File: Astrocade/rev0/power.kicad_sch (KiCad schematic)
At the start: 10 parts, among them U5 AP63203WU

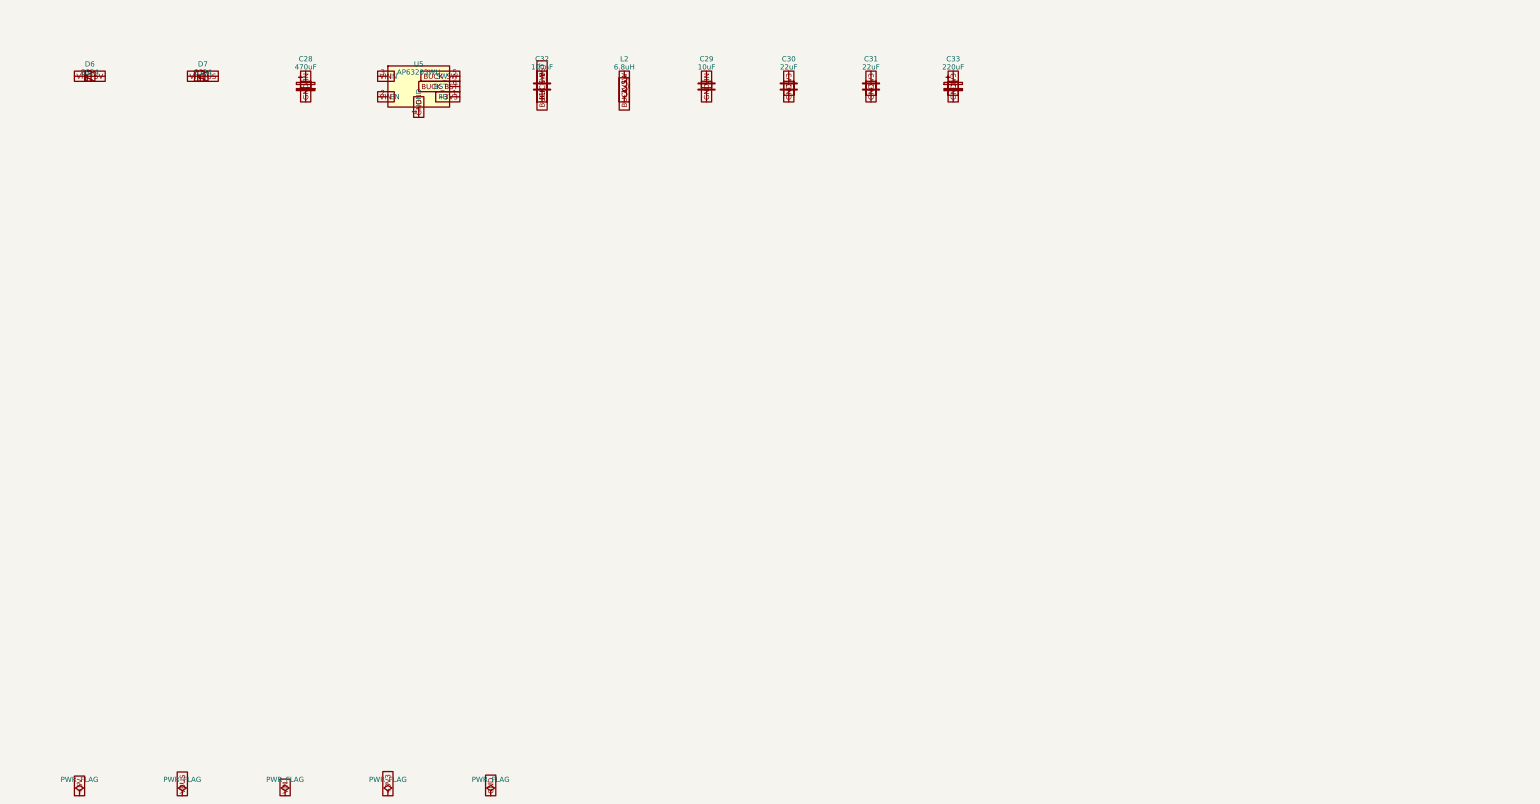
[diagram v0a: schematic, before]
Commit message: Astrocade Rev0: redo on RP2354A + ESP32-S3, 6-layer, fully autorouted
Replaces the unrouted RP2040 + 3x LVC245 draft with an INTV-style board:
RP2354A straight on the 5V bus, ESP32-S3-WROOM-1-N16R8 as its USB host
(PICOBOOT reflash), USB-C/CP2102N, push-push microSD, WS2812B-2020-V6,
RESET/BOOTSEL/EN/BOOT buttons. Same cassette outline, lands and holes.

Everything is generated by tools/ (build_all.sh): design.py -> schematic,
placement + plane fan-out, Raspberry Pi's MIT regulator-corner graft,
Freerouting + A* finisher, netlist-vs-firmware check, JLCPCB BOM/CPL/gerbers.
ERC 0, DRC 0 errors / 0 unconnected / 0 parity, check_nets 174/174.

RUN/BOOTSEL from the S3 are direct 1k links (fnPicoUpdater drives them low;
an NPN driver would invert it). Shell openings come from the placement.

Co-Authored-By: Claude Opus 5.5 (1M context) <noreply@anthropic.com>
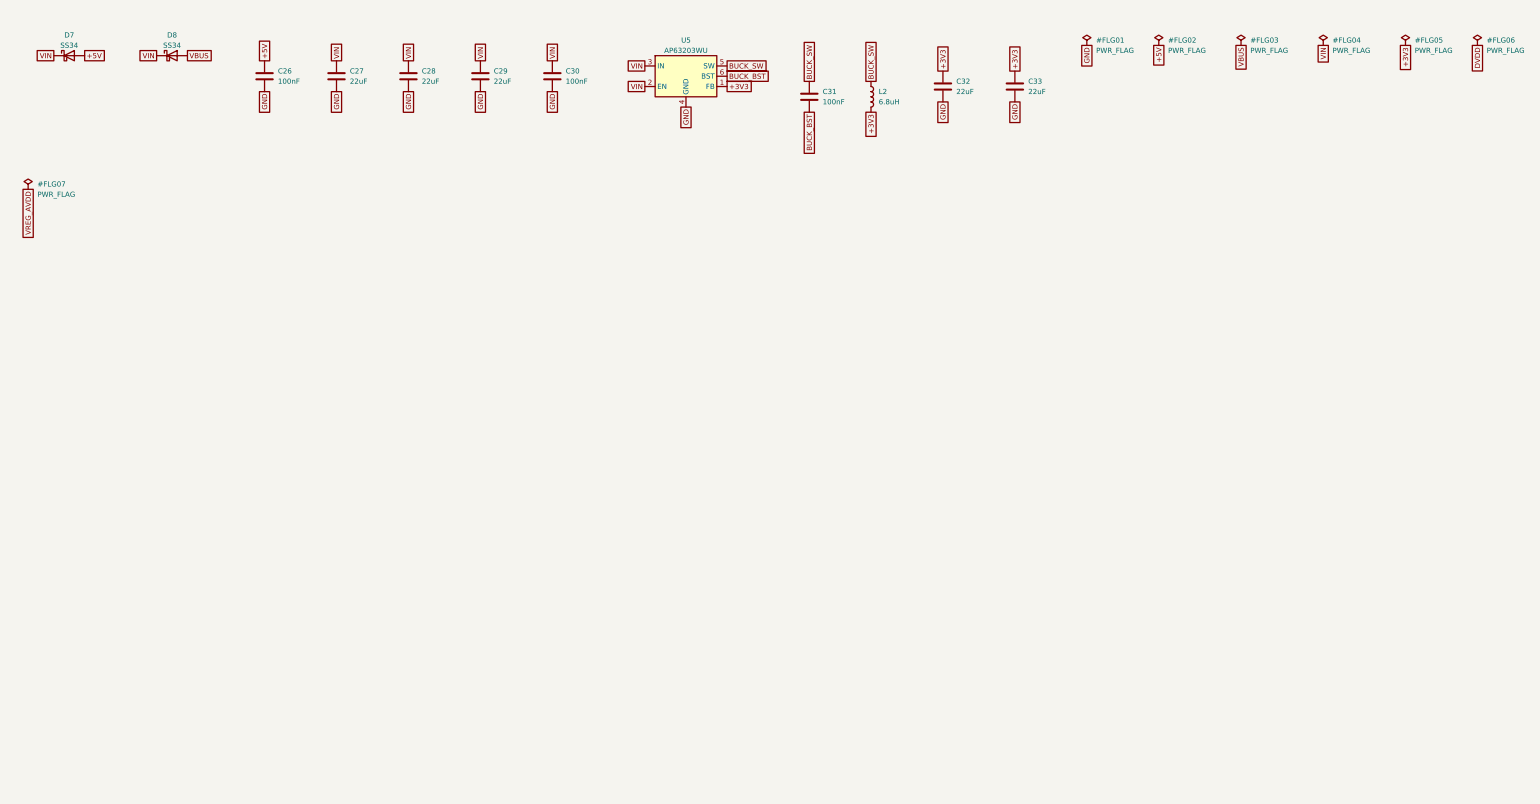
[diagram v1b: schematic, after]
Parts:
- removed C28: 470uF, FujiNet-Astrocade:CP_EIA-7343-31_Kemet-D, symbol Device:C_Polarized
- removed C33: 220uF, FujiNet-Astrocade:CP_EIA-7343-31_Kemet-D, symbol Device:C_Polarized
- removed D6: SS34, FujiNet-Astrocade:D_SMA, symbol Diode:SS34
- added C26: 100nF, FujiNet-Astrocade:C_0603_1608Metric, symbol Device:C
- added C27, C28, C33: 22uF, FujiNet-Astrocade:C_0805_2012Metric, symbol Device:C
- added D8: SS34, FujiNet-Astrocade:D_SMA, symbol Diode:SS34
- C29: value 10uF -> 22uF; LCSC (none) -> C45783; MPN (none) -> CL21A226MAQNNNE
- C30, C31: value 22uF -> 100nF; footprint FujiNet-Astrocade:C_0805_2012Metric -> FujiNet-Astrocade:C_0603_1608Metric; LCSC C45783 -> C14663; MPN (none) -> CC0603KRX7R9BB104
- C32: value 100nF -> 22uF; footprint FujiNet-Astrocade:C_0603_1608Metric -> FujiNet-Astrocade:C_0805_2012Metric; LCSC (none) -> C45783; MPN (none) -> CL21A226MAQNNNE
- D7: MPN (none) -> SS34
- L2: LCSC (none) -> C62684; MPN 6.8uH >=2.5A shielded 4030 -> SWPA4030S6R8MT
- U5: LCSC C965680 -> C780769
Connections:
- net +3V3: now also C32.1, C33.1; no longer C30.1, C31.1
- net +5V: now also D7.2 (A), C26.1
- net BUCK_BST: now also C31.2; no longer C32.2
- net BUCK_SW: now also C31.1; no longer C32.1
- net GND: now also C32.2, C26.2, C27.2, C28.2, C33.2; no longer C31.2
- net VBUS: now also D8.2 (A); no longer D7.2 (A)
- net VIN: now also C30.1, C27.1, C28.1, D8.1 (K)
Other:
- company: (none) -> FujiNet
- title: (none) -> FujiNet Astrocade Rev0 - Power: console 5V / USB VBUS OR, 3.3V buck

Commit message: Astrocade Rev0: audit with kicad-happy + datasheets and redo
Schematic, board and fab outputs regenerated from tools/ after a
datasheet-level audit (docs/design-review-rev0.md).

Design fixes:
- RP2354A on its own AP2112K rail (+3V3_RP): its FT pads take 5.5 V only
  with IOVDD powered (RP2350 DS p.1332); the buck's UVLO + 4 ms soft-start
  left them unpowered while the console drove the bus
- WS2812B-2020-V6 on +5V (datasheet VDD 3.7-5.3 V, not a 3.3 V part)
- VBUS decoupling at the USB-C, activity LED 330R, card-detect polarity
  settled (low = card present), fiducials, RUN/BOOTSEL/rail test pads

Schematic redrawn readably: root block diagram with hierarchical pins,
power symbols, wired clusters and design notes (tools/sch_layout.py);
check_sch_layout.py proves the drawn netlist equals design.py.

Board: 4 layers tried first and did not close; 6 layers, 100% routed,
DRC 0 errors / 0 unconnected / 0 parity. Locked USB-C D+/D- pad ties,
GND stitching kept out of pads, return vias at USB/crystal layer
changes, check_vias.py gate (KiCad re-nets a via inside another net's
pad, so its DRC cannot see it).

Co-Authored-By: Claude Opus 5.5 <noreply@anthropic.com>
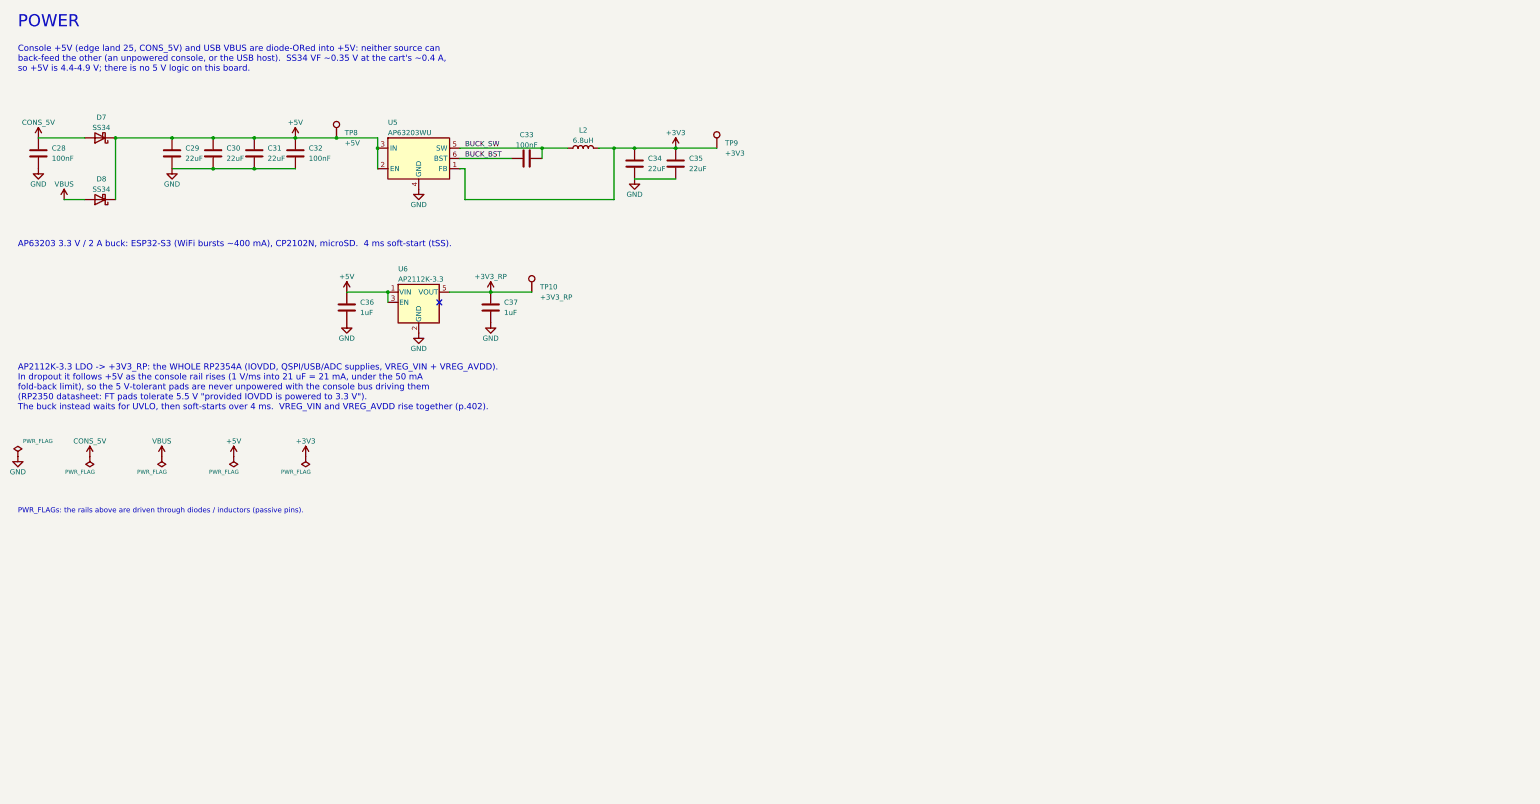
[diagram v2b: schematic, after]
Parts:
- removed C26: 100nF, FujiNet-Astrocade:C_0603_1608Metric, symbol Device:C
- removed C27: 22uF, FujiNet-Astrocade:C_0805_2012Metric, symbol Device:C
- added C34, C35: 22uF, FujiNet-Astrocade:C_0805_2012Metric, symbol Device:C
- added C36, C37: 1uF, FujiNet-Astrocade:C_0603_1608Metric, symbol Device:C
- added TP10: +3V3_RP, FujiNet-Astrocade:TestPoint_Pad_D1.5mm, symbol Connector:TestPoint
- added TP8: +5V, FujiNet-Astrocade:TestPoint_Pad_D1.5mm, symbol Connector:TestPoint
- added TP9: +3V3, FujiNet-Astrocade:TestPoint_Pad_D1.5mm, symbol Connector:TestPoint
- added U6: AP2112K-3.3, FujiNet-Astrocade:SOT-23-5, symbol Regulator_Linear:AP2112K-3.3
- C28, C32, C33: value 22uF -> 100nF; footprint FujiNet-Astrocade:C_0805_2012Metric -> FujiNet-Astrocade:C_0603_1608Metric; LCSC C45783 -> C14663; MPN CL21A226MAQNNNE -> CC0603KRX7R9BB104
- C30, C31: value 100nF -> 22uF; footprint FujiNet-Astrocade:C_0603_1608Metric -> FujiNet-Astrocade:C_0805_2012Metric; LCSC C14663 -> C45783; MPN CC0603KRX7R9BB104 -> CL21A226MAQNNNE
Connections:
- net +3V3: now also C34.1, C35.1, TP9.1; no longer C32.1, C33.1
- net +5V: now also C29.1, C30.1, C31.1, C32.1, D7.1 (K), D8.1 (K), U5.2 (EN), U5.3 (IN), C36.1, TP8.1, U6.1 (VIN), U6.3 (EN); no longer D7.2 (A)
- net BUCK_BST: now also C33.2; no longer C31.2
- net BUCK_SW: now also C33.1; no longer C31.1
- net GND: now also C31.2, C34.2, C35.2, C36.2, C37.2, U6.2 (GND); no longer C33.2
- removed net VIN: C28.1, C29.1, C30.1, D7.1 (K), D8.1 (K), U5.2 (EN), U5.3 (IN)
- new net +3V3_RP: C37.1, TP10.1, U6.5 (VOUT)
- new net CONS_5V: C28.1, D7.2 (A)
- no-connect marks 0 -> 1
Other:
- note added: "AP2112K-3.3 LDO -> +3V3_RP: the WHOLE RP2354A (IOVDD, QSPI/USB/ADC supplies, VREG_VIN + VREG_AVDD). In dropout it follows +5V as the console rail rises (1 V/ms into 21 uF = 21 mA, under the 50 mA fold-back limit), so the 5 V-tolerant pads are never unpowered with the console bus driving them (RP2350 datasheet: FT pads tolerate 5.5 V "provided IOVDD is powered to 3.3 V"). The buck instead waits fo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"
- note added: "AP63203 3.3 V / 2 A buck: ESP32-S3 (WiFi bursts ~400 mA), CP2102N, microSD. 4 ms soft-start (tSS)."
- note added: "Console +5V (edge land 25, CONS_5V) and USB VBUS are diode-ORed into +5V: neither source can back-feed the other (an unpowered console, or the USB host). SS34 VF ~0.35 V at the cart's ~0.4 A, so +5V is 4.4-4.9 V; there is no 5 V logic on this board."
- note added: "POWER"
- note added: "PWR_FLAGs: the rails above are driven through diodes / inductors (passive pins)."
- title: FujiNet Astrocade Rev0 - Power: console 5V / USB VBUS OR, 3.3V buck -> FujiNet Astrocade Rev0 - Power: console 5V / USB VBUS OR, 3.3V buck, RP 3.3V LDO
- moved on the sheet: C28, C29, C30, C31, C32, C33, D7, D8, L2, U5

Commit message: Astrocade Rev0: redraw the schematic wired (5200 style), re-audit (#53)
The schematic was readable but disconnected: every edge land and RP GPIO
ended in a label and the RP's decoupling stood in a row away from its pins.
Port the FujiNet-5200 drawing pipeline (sch_draw / sch_draft / sch_place /
netlist) and hand-draw every sheet the way the later carts are drawn:

- root: the board outline at 2:1, each sheet's block over its region, the
  nine inter-sheet signals wired without a crossing
- cart-bus: the 26-land edge straight into the RP2354A's GPIO unit
  (22 parallel wires, no crossings); rp-core: every supply pin wired to
  its own capacitor and rail; fujinet, usb, power: all wired
- RP2354A split into two units; references frozen in tools/refs.lock,
  net names in tools/nets.lock

The routed board is unchanged: tools/sync_pcb_nets.py renames the board's
nets to the new sheet paths (self-checked), sync_pcb_sheets.py re-points
the footprint links. DRC with schematic parity 0/0/0, ERC 0, netlist
parity 74/74, check_nets 182/182; CPL byte-identical, gerbers identical
but for names and dates. build_all.sh now keeps the routed board by
default (LAYOUT=1 re-routes).

Re-audit (design review Part 3, deep review 25/25 gated, datasheets from
the sibling carts): VSENSE divider 100k/150k -> 10k/15k so RP2350-E9 (A2
silicon) cannot hold the serve gate open in a switched-off console (value
change only, same lands). DVDD decoupling, a VBUS pull-down, the activity
LED and the core inductor's stock are Rev1 / bring-up notes.

Co-authored-by: Claude Opus 5.5 <noreply@anthropic.com>
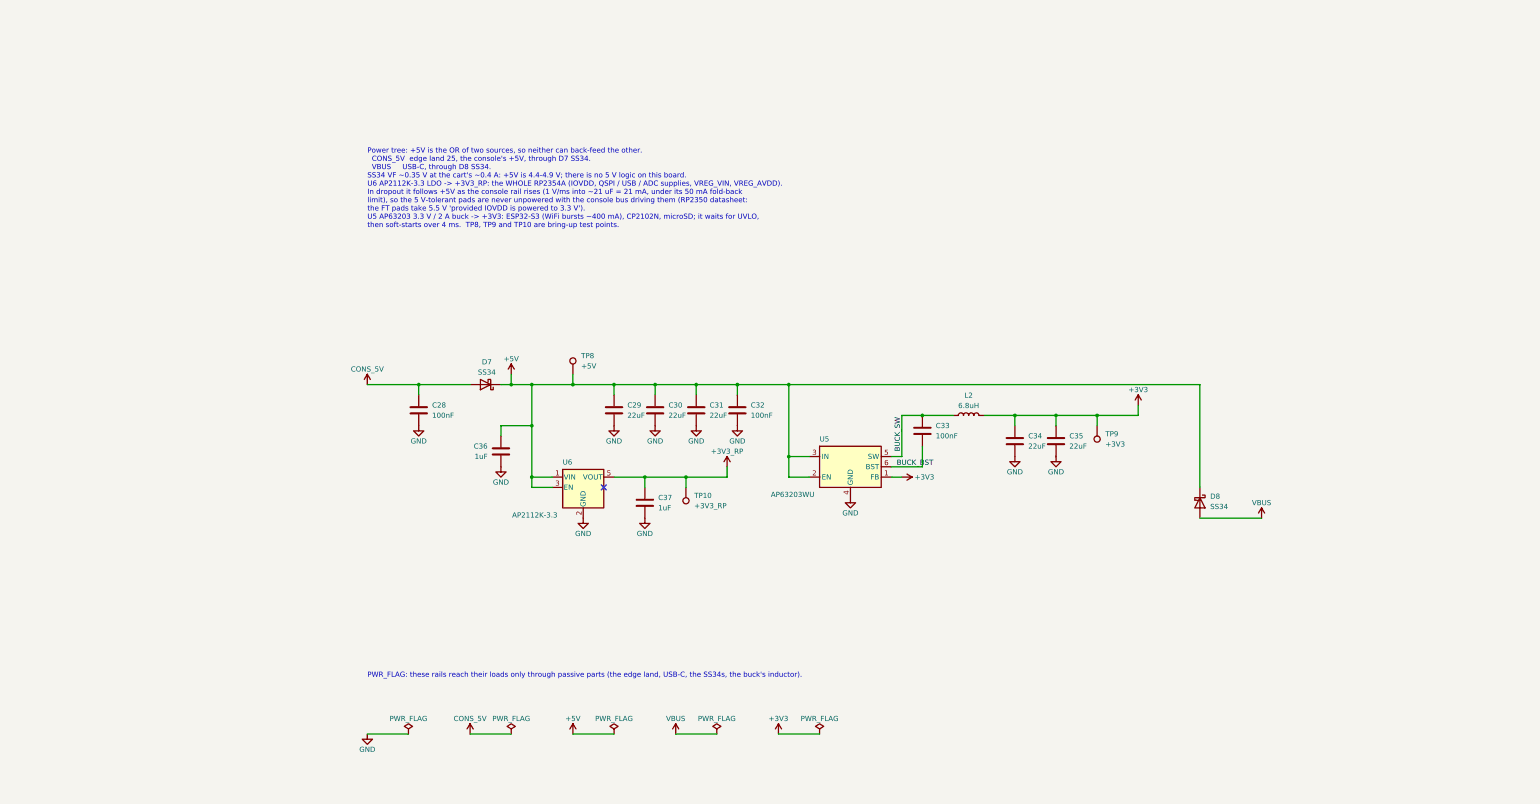
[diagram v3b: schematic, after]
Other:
- note added: "PWR_FLAG: these rails reach their loads only through passive parts (the edge land, USB-C, the SS34s, the buck's inductor)."
- note added: "Power tree: +5V is the OR of two sources, so neither can back-feed the other. CONS_5V edge land 25, the console's +5V, through D7 SS34. VBUS USB-C, through D8 SS34. SS34 VF ~0.35 V at the cart's ~0.4 A: +5V is 4.4-4.9 V; there is no 5 V logic on this board. U6 AP2112K-3.3 LDO -> +3V3_RP: the WHOLE RP2354A (IOVDD, QSPI / USB / ADC supplies, VREG_VIN, VREG_AVDD). In dropout it follows +5V as the co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"
- note removed: "AP2112K-3.3 LDO -> +3V3_RP: the WHOLE RP2354A (IOVDD, QSPI/USB/ADC supplies, VREG_VIN + VREG_AVDD). In dropout it follows +5V as the console rail rises (1 V/ms into 21 uF = 21 mA, under the 50 mA fold-back limit), so the 5 V-tolerant pads are never unpowered with the console bus driving them (RP2350 datasheet: FT pads tolerate 5.5 V "provided IOVDD is powered to 3.3 V"). The buck instead waits fo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"
- note removed: "AP63203 3.3 V / 2 A buck: ESP32-S3 (WiFi bursts ~400 mA), CP2102N, microSD. 4 ms soft-start (tSS)."
- note removed: "Console +5V (edge land 25, CONS_5V) and USB VBUS are diode-ORed into +5V: neither source can back-feed the other (an unpowered console, or the USB host). SS34 VF ~0.35 V at the cart's ~0.4 A, so +5V is 4.4-4.9 V; there is no 5 V logic on this board."
- note removed: "POWER"
- note removed: "PWR_FLAGs: the rails above are driven through diodes / inductors (passive pins)."
- title: FujiNet Astrocade Rev0 - Power: console 5V / USB VBUS OR, 3.3V buck, RP 3.3V LDO -> FujiNet Astrocade Rev0 - Power: 5V OR, 3.3V buck, RP LDO
- moved on the sheet: C28, C29, C30, C31, C32, C33, C34, C35, C36, C37, D7, D8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
